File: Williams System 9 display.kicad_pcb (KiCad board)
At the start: 4 copper layers, 96.3 x 53.2 mm, 30 parts, among them J101 Conn_01x02, J102 Conn_01x08, J103 Conn_01x08, J104 Conn_01x03, J105 Conn_01x04, J106 Conn_01x04, U101 74HC148, U102 74LV08A, U103 Pico, U104 74HC148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

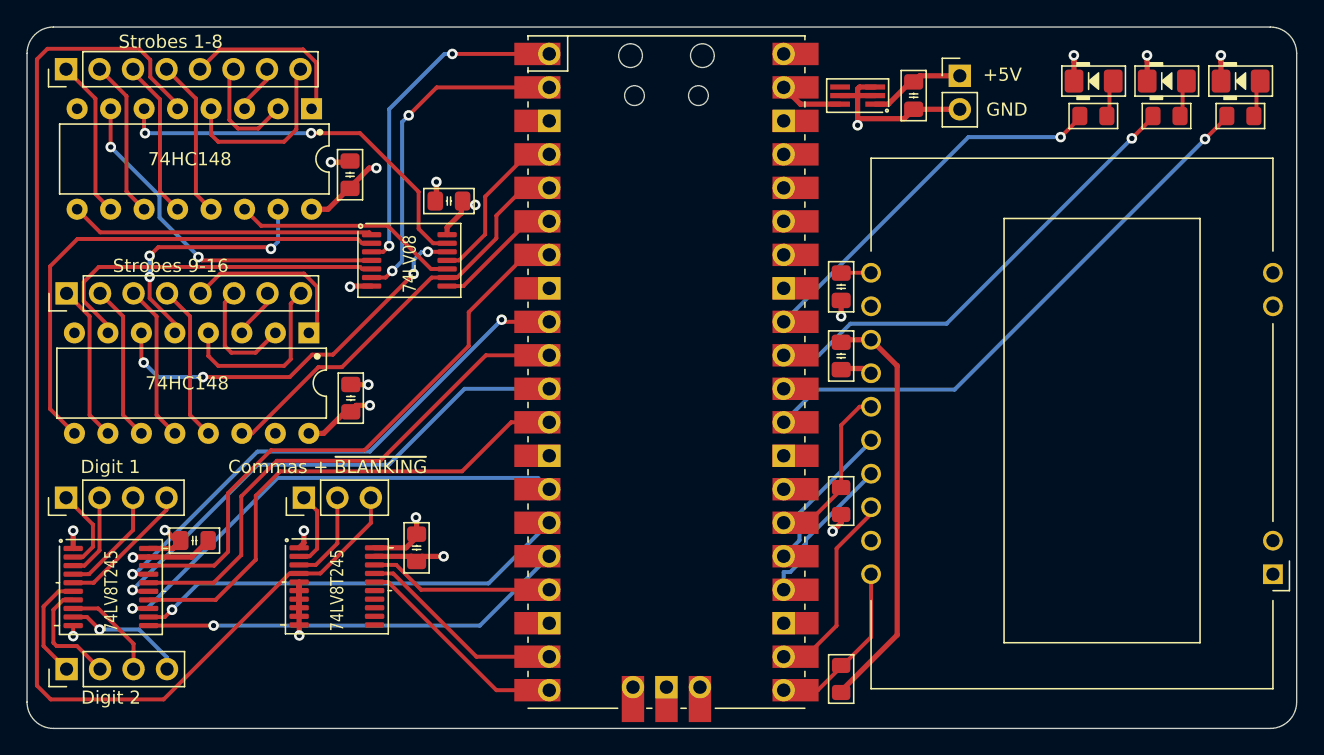
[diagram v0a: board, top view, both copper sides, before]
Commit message: More informative silkscreen
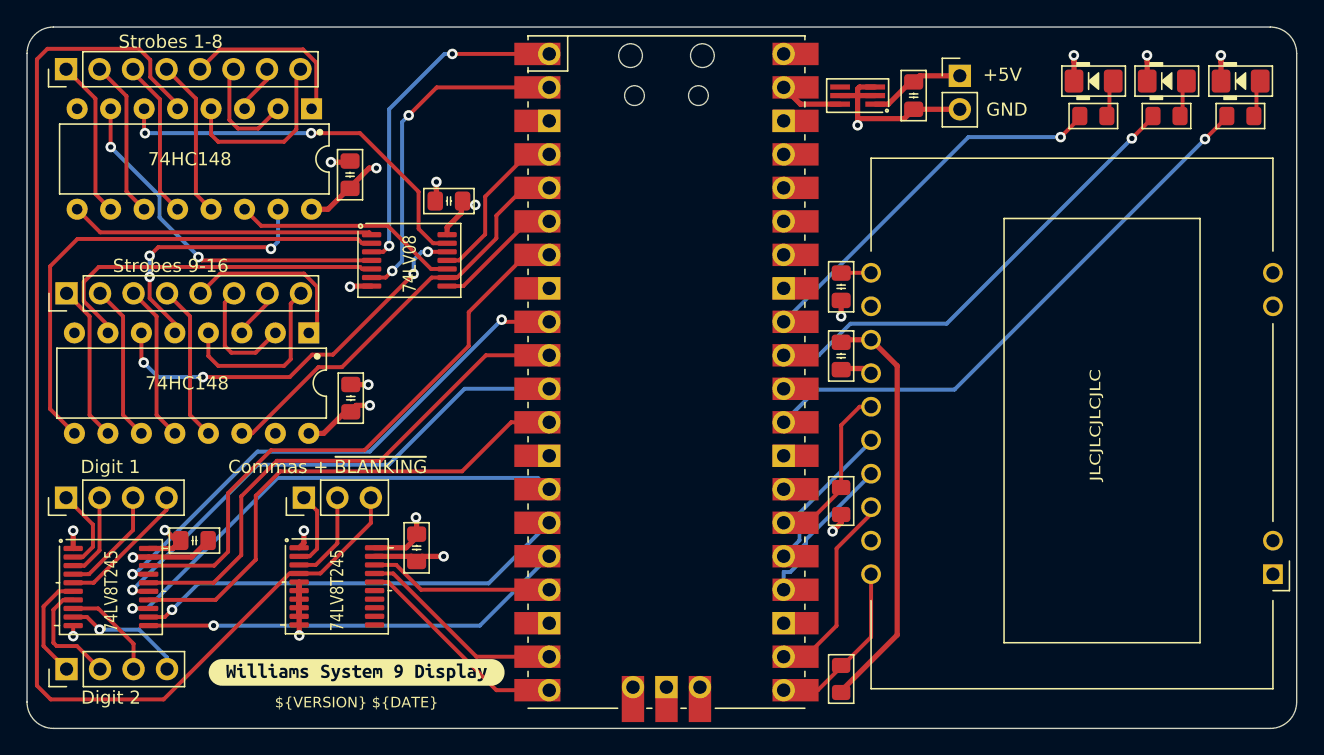
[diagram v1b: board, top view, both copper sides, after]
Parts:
- added kibuzzard-64FB800B: G***, kibuzzard-64FB800B, F.Cu at (200.0, 98.8)
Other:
- board text added: "${VERSION} ${DATE}"
- board text added: "JLCJLCJLCJLC"
